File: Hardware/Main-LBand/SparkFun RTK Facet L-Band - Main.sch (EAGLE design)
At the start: 131 parts, among them J1 QWIIC_RIGHT_ANGLE, J10 FPC_12_0.5MM_BACKFLIP, J15 FPC_12_0.5MM_BACKFLIP, J18 FPC_12_0.5MM_BACKFLIP, J2 U.FL, J8 FPC_12_0.5MM_BACKFLIP, J9 CORTEX_JTAG_DEBUG_PTH, Q2 MBT3904DW1T1, Q3 SIL2308, U1 74HC4052D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

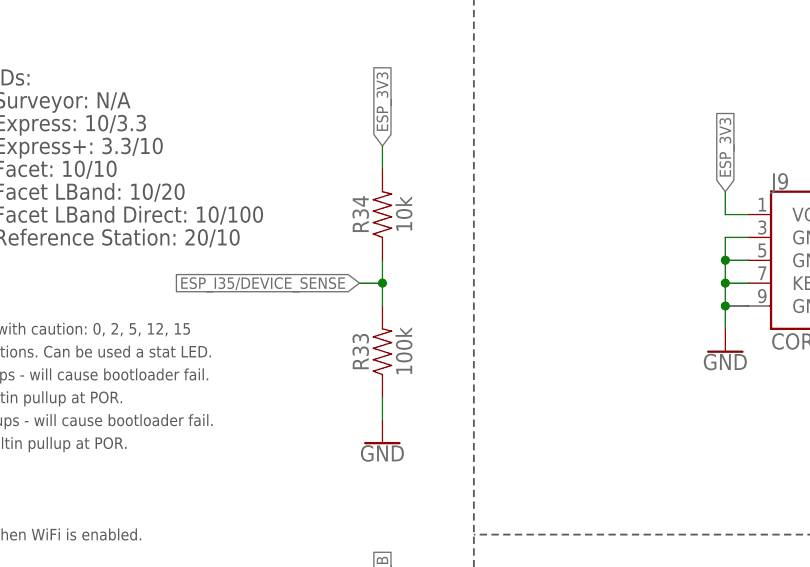
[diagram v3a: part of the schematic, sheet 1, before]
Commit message: Update ID resistors.
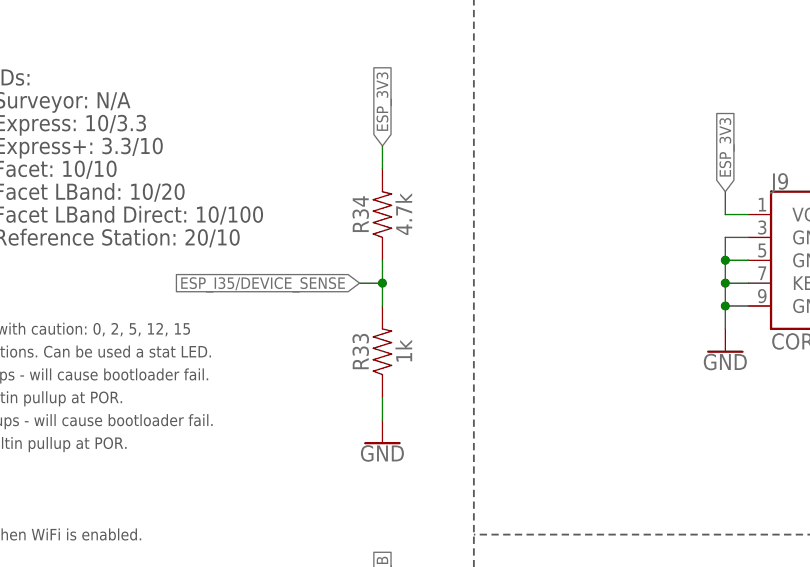
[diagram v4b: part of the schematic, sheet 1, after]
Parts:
- R33: value 100k -> 1k; device SparkFun-Resistors:100KOHM-0603-1/10W-1% -> SparkFun-Resistors:1KOHM-0603-1/10W-1%
- R34: value 10k -> 4.7k; device SparkFun-Resistors:10KOHM-0603-1/10W-1% -> SparkFun-Resistors:4.7KOHM-0603-1/10W-1%
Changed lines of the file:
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@@
 <grid distance="0.1" unitdist="inch" unit="inch" style="lines" multiple="1" display="no" altdistance="0.01" altunitdist="inch" altunit="inch"/>
 <layers>
-<layer number="1" name="Top" color="4" fill="1" visible="yes" active="no"/>
-<layer number="2" name="Route2" color="1" fill="3" visible="yes" active="no"/>
-<layer number="3" name="Route3" color="4" fill="3" visible="yes" active="no"/>
-<layer number="4" name="Route4" color="1" fill="4" visible="yes" active="no"/>
-<layer number="5" name="Route5" color="4" fill="4" visible="yes" active="no"/>
-<layer number="6" name="Route6" color="1" fill="8" visible="yes" active="no"/>
-<layer number="7" name="Route7" color="4" fill="8" visible="yes" active="no"/>
-<layer number="8" name="Route8" color="1" fill="2" visible="yes" active="no"/>
-<layer number="9" name="Route9" color="4" fill="2" visible="yes" active="no"/>
-<layer number="10" name="Route10" color="1" fill="7" visible="yes" active="no"/>
-<layer number="11" name="Route11" color="4" fill="7" visible="yes" active="no"/>
-<layer number="12" name="Route12" color="1" fill="5" visible="yes" active="no"/>
-<layer number="13" name="Route13" color="4" fill="5" visible="yes" active="no"/>
-<layer number="14" name="Route14" color="1" fill="6" visible="yes" active="no"/>
-<layer number="15" name="Route15" color="4" fill="6" visible="yes" active="no"/>
-<layer number="16" name="Bottom" color="1" fill="1" visible="yes" active="no"/>
-<layer number="17" name="Pads" color="2" fill="1" visible="yes" active="no"/>
-<layer number="18" name="Vias" color="2" fill="1" visible="yes" active="no"/>
-<layer number="19" name="Unrouted" color="6" fill="1" visible="yes" active="no"/>
-<layer number="20" name="Dimension" color="24" fill="1" visible="yes" active="no"/>
-<layer number="21" name="tPlace" color="16" fill="1" visible="yes" active="no"/>
-<layer number="22" name="bPlace" color="14" fill="1" visible="yes" active="no"/>
-<layer number="23" name="tOrigins" color="15" fill="1" visible="yes" active="no"/>
-<layer number="24" name="bOrigins" color="15" fill="1" visible="yes" active="no"/>
-<layer number="25" name="tNames" color="7" fill="1" visible="yes" active="no"/>
-<layer number="26" name="bNames" color="7" fill="1" visible="yes" active="no"/>
-<layer number="27" name="tValues" color="7" fill="1" visible="yes" active="no"/>
-<layer number="28" name="bValues" color="7" fill="1" visible="yes" active="no"/>
+<layer number="1" name="Top" color="4" fill="1" visible="no" active="no"/>
+<layer number="2" name="Route2" color="1" fill="3" visible="no" active="no"/>
+<layer number="3" name="Route3" color="4" fill="3" visible="no" active="no"/>
+<layer number="4" name="Route4" color="1" fill="4" visible="no" active="no"/>
+<layer number="5" name="Route5" color="4" fill="4" visible="no" active="no"/>
+<layer number="6" name="Route6" color="1" fill="8" visible="no" active="no"/>
+<layer number="7" name="Route7" color="4" fill="8" visible="no" active="no"/>
+<layer number="8" name="Route8" color="1" fill="2" visible="no" active="no"/>
+<layer number="9" name="Route9" color="4" fill="2" visible="no" active="no"/>
+<layer number="10" name="Route10" color="1" fill="7" visible="no" active="no"/>
+<layer number="11" name="Route11" color="4" fill="7" visible="no" active="no"/>
+<layer number="12" name="Route12" color="1" fill="5" visible="no" active="no"/>
+<layer number="13" name="Route13" color="4" fill="5" visible="no" active="no"/>
+<layer number="14" name="Route14" color="1" fill="6" visible="no" active="no"/>
+<layer number="15" name="Route15" color="4" fill="6" visible="no" active="no"/>
+<layer number="16" name="Bottom" color="1" fill="1" visible="no" active="no"/>
+<layer number="17" name="Pads" color="2" fill="1" visible="no" active="no"/>
+<layer number="18" name="Vias" color="2" fill="1" visible="no" active="no"/>
+<layer number="19" name="Unrouted" color="6" fill="1" visible="no" active="no"/>
+<layer number="20" name="Dimension" color="24" fill="1" visible="no" active="no"/>
+<layer number="21" name="tPlace" color="16" fill="1" visible="no" active="no"/>
+<layer number="22" name="bPlace" color="14" fill="1" visible="no" active="no"/>
+<layer number="23" name="tOrigins" color="15" fill="1" visible="no" active="no"/>
+<layer number="24" name="bOrigins" color="15" fill="1" visible="no" active="no"/>
+<layer number="25" name="tNames" color="7" fill="1" visible="no" active="no"/>
+<layer number="26" name="bNames" color="7" fill="1" visible="no" active="no"/>
+<layer number="27" name="tValues" color="7" fill="1" visible="no" active="no"/>
+<layer number="28" name="bValues" color="7" fill="1" visible="no" active="no"/>
 <layer number="29" name="tStop" color="7" fill="3" visible="no" active="no"/>
 <layer number="30" name="bStop" color="7" fill="6" visible="no" active="no"/>
@@
 <layer number="35" name="tGlue" color="7" fill="4" visible="no" active="no"/>
 <layer number="36" name="bGlue" color="7" fill="5" visible="no" active="no"/>
-<layer number="37" name="tTest" color="7" fill="1" visible="yes" active="no"/>
-<layer number="38" name="bTest" color="7" fill="1" visible="yes" active="no"/>
+<layer number="37" name="tTest" color="7" fill="1" visible="no" active="no"/>
+<layer number="38" name="bTest" color="7" fill="1" visible="no" active="no"/>
 <layer number="39" name="tKeepout" color="4" fill="11" visible="no" active="no"/>
 <layer number="40" name="bKeepout" color="1" fill="11" visible="no" active="no"/>
@@
 <layer number="44" name="Drills" color="7" fill="1" visible="no" active="no"/>
 <layer number="45" name="Holes" color="7" fill="1" visible="no" active="no"/>
-<layer number="46" name="Milling" color="3" fill="1" visible="yes" active="no"/>
-<layer number="47" name="Measures" color="7" fill="1" visible="yes" active="no"/>
-<layer number="48" name="Document" color="7" fill="1" visible="yes" active="no"/>
-<layer number="49" name="Reference" color="7" fill="1" visible="yes" active="no"/>
-<layer number="50" name="dxf" color="7" fill="1" visible="yes" active="no"/>
-<layer number="51" name="tDocu" color="6" fill="1" visible="yes" active="no"/>
-<layer number="52" name="bDocu" color="7" fill="1" visible="yes" active="no"/>
-<layer number="53" name="tGND_GNDA" color="7" fill="9" visible="yes" active="no"/>
-<layer number="54" name="bGND_GNDA" color="1" fill="9" visible="yes" active="no"/>
-<layer number="56" name="wert" color="7" fill="1" visible="yes" active="no"/>
-<layer number="57" name="tCAD" color="7" fill="1" visible="yes" active="no"/>
-<layer number="58" name="bCAD" color="7" fill="1" visible="yes" active="no"/>
-<layer number="59" name="tCarbon" color="7" fill="1" visible="yes" active="no"/>
-<layer number="60" name="bCarbon" color="7" fill="1" visible="yes" active="no"/>
+<layer number="46" name="Milling" color="3" fill="1" visible="no" active="no"/>
+<layer number="47" name="Measures" color="7" fill="1" visible="no" active="no"/>
+<layer number="48" name="Document" color="7" fill="1" visible="no" active="no"/>
+<layer number="49" name="Reference" color="7" fill="1" visible="no" active="no"/>
+<layer number="50" name="dxf" color="7" fill="1" visible="no" active="no"/>
+<layer number="51" name="tDocu" color="6" fill="1" visible="no" active="no"/>
+<layer number="52" name="bDocu" color="7" fill="1" visible="no" active="no"/>
+<layer number="53" name="tGND_GNDA" color="7" fill="9" visible="no" active="no"/>
+<layer number="54" name="bGND_GNDA" color="1" fill="9" visible="no" active="no"/>
+<layer number="56" name="wert" color="7" fill="1" visible="no" active="no"/>
+<layer number="57" name="tCAD" color="7" fill="1" visible="no" active="no"/>
+<layer number="58" name="bCAD" color="7" fill="1" visible="no" active="no"/>
+<layer number="59" name="tCarbon" color="7" fill="1" visible="no" active="no"/>
+<layer number="60" name="bCarbon" color="7" fill="1" visible="no" active="no"/>
 <layer number="88" name="SimResults" color="9" fill="1" visible="yes" active="yes"/>
 <layer number="89" name="SimProbes" color="9" fill="1" visible="yes" active="yes"/>
@@
 <part name="J9" library="SparkFun-Connectors" deviceset="CORTEX_JTAG_DEBUG" device="_PTH"/>
 <part name="GND17" library="SparkFun-PowerSymbols" deviceset="GND" device=""/>
-<part name="R33" library="SparkFun-Resistors" deviceset="100KOHM" device="-0603-1/10W-1%" value="100k"/>
-<part name="R34" library="SparkFun-Resistors" deviceset="10KOHM" device="-0603-1/10W-1%" value="10k"/>
+<part name="R33" library="SparkFun-Resistors" deviceset="1KOHM" device="-0603-1/10W-1%" value="1k"/>
+<part name="R34" library="SparkFun-Resistors" deviceset="4.7KOHM" device="-0603-1/10W-1%" value="4.7k"/>
 <part name="GND26" library="SparkFun-PowerSymbols" deviceset="GND" device=""/>
 <part name="SUPPLY13" library="SparkFun-PowerSymbols" deviceset="3.3V" device=""/>

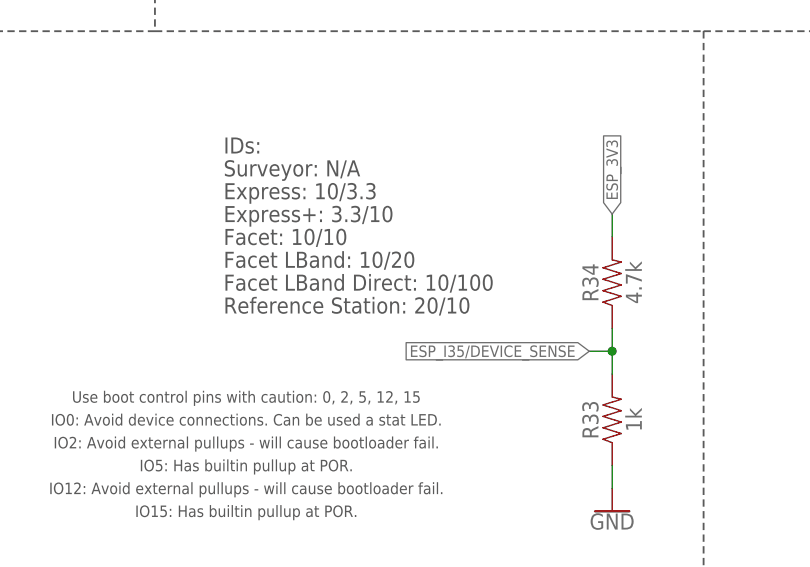
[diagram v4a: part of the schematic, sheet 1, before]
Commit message: Update ID resistors
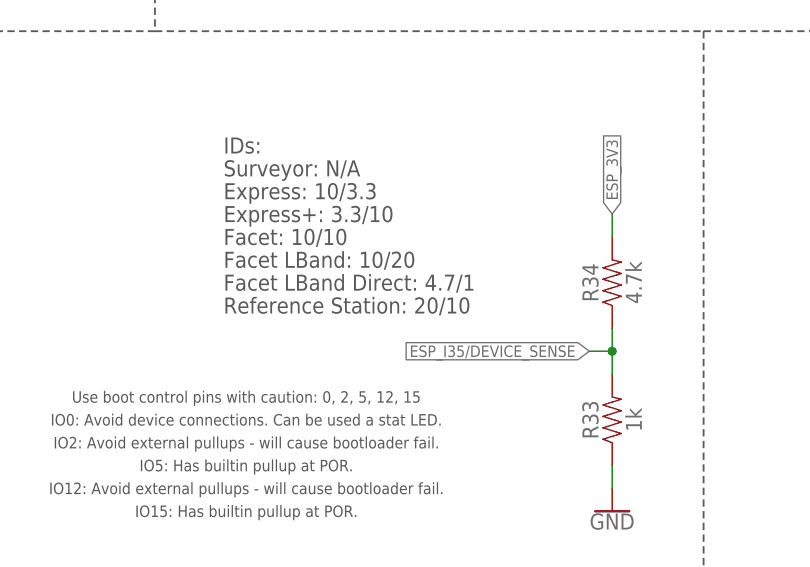
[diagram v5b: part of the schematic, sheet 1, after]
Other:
- note added: "Facet LBand Direct: 4.7/1"
- note removed: "Facet LBand Direct: 10/100"
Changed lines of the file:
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@@
 <text x="276.86" y="101.6" size="1.778" layer="97" align="center-left">Facet LBand: 10/20</text>
 <text x="220.98" y="185.42" size="1.778" layer="97" align="center">7-bit unshifted I²C address: 0x36</text>
-<text x="276.86" y="99.06" size="1.778" layer="97" align="center-left">Facet LBand Direct: 10/100</text>
+<text x="276.86" y="99.06" size="1.778" layer="97" align="center-left">Facet LBand Direct: 4.7/1</text>
 <text x="276.86" y="96.52" size="1.778" layer="97" align="center-left">Reference Station: 20/10</text>
 </plain>
